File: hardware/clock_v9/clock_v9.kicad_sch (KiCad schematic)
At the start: 176 parts, among them J1 RJ45, J12 Conn_01x06, J14 DC-063-25A, J4 USB_C_Receptacle, J5 Conn_01x06_Pin, J6 Conn_01x04_Pin, J8 Conn_01x02, Q1 2N7002, Q10 2N7002, Q2 S8550, Q3 S8050, Q4 S8050, Q5 S8050, Q9 2N7002, SW1 LC1258OASP, U1 ADA4807-1, U10 STM32F405RGTx, U11 AMS1117-3.3, U12 BA50DD0WHFP-TR, U13 M24C02-RMN, U14 CH340C, U15 USBLC6-2P6, U16 TLV3603DCKR, U17 SN74LVC1G14DBV, U2 SN74LVC1G14DBV, U3 SN74LVC1G14DBV, U4 ADA4807-1, U5 ADA4807-1, U6 TLV3603DCKR, U7 SN74LVC1G14DBV, U8 TLV3603DCKR, U9 L78L05_SOT89, Y1 AOCJY4A-10.000MHZ-SW, Y2 16MHz

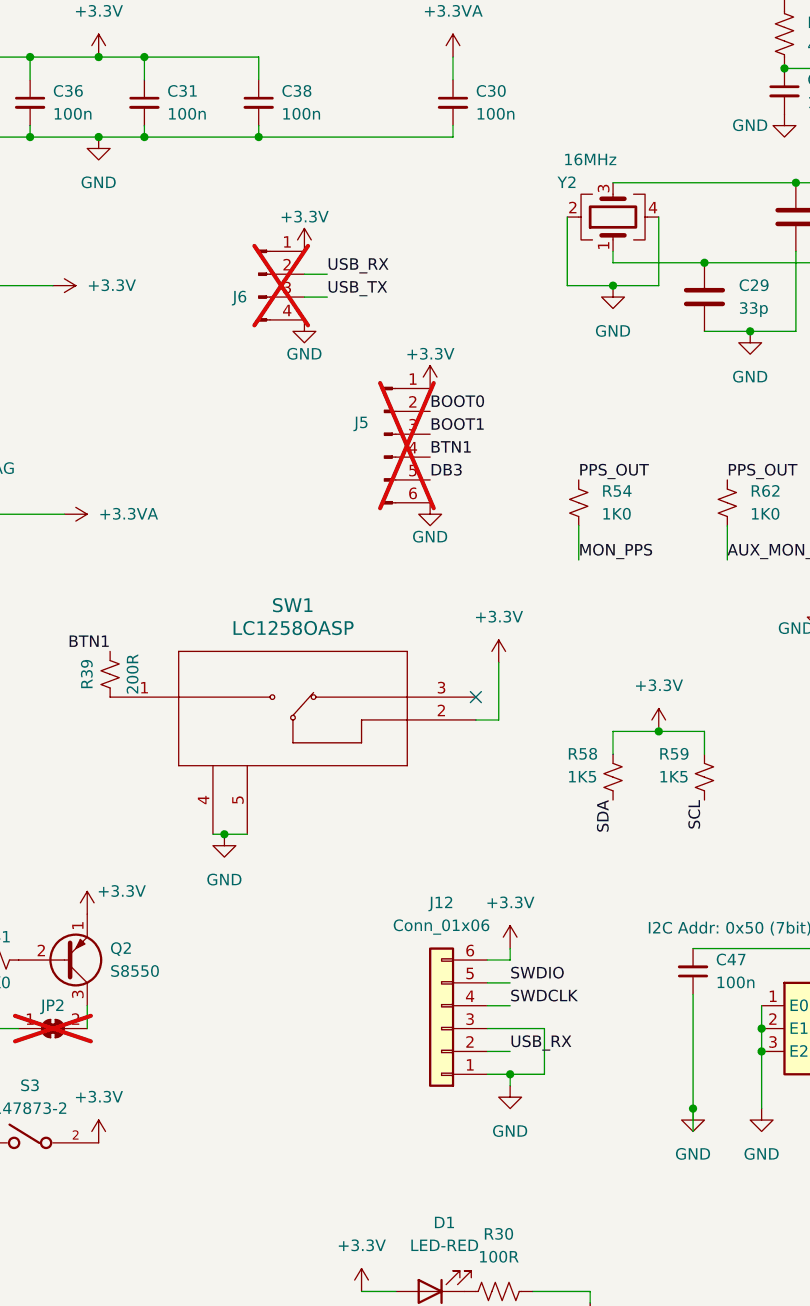
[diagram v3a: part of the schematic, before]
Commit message: update jumpers and swtiches
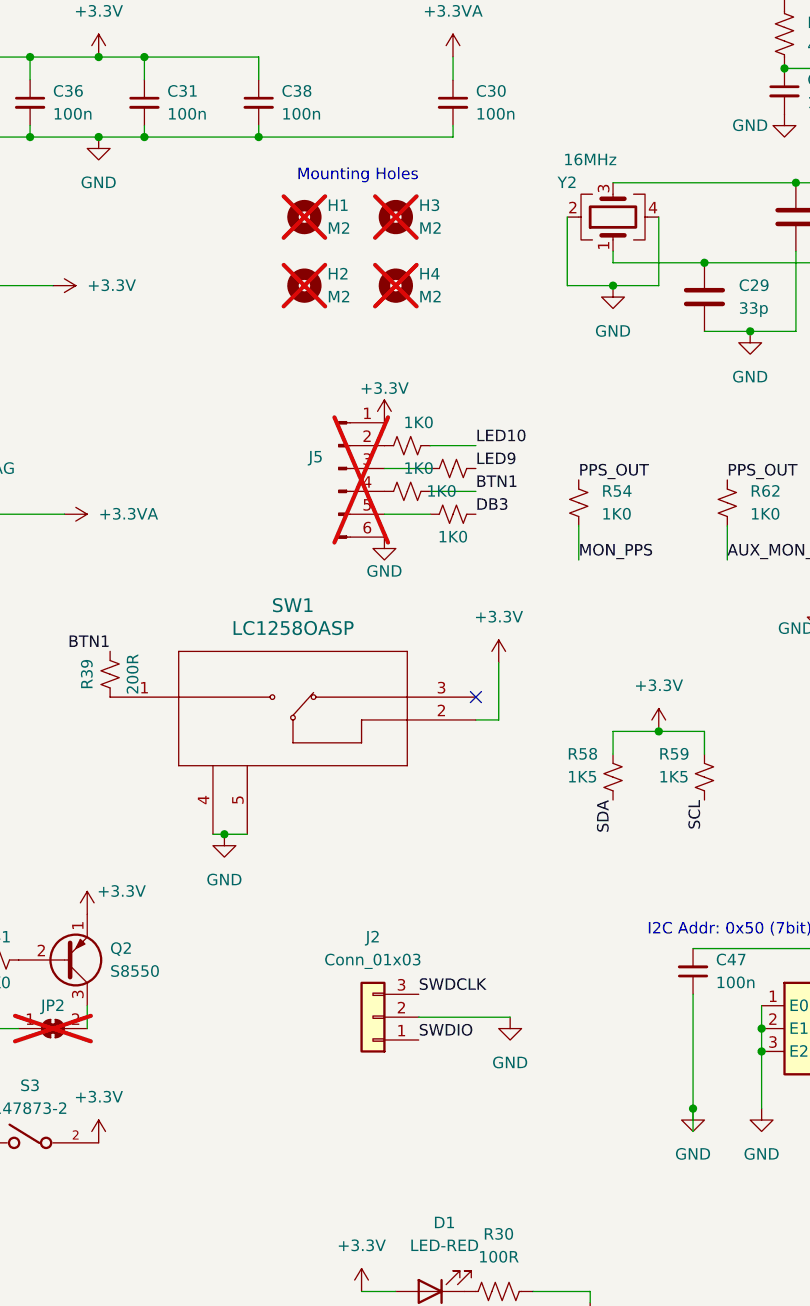
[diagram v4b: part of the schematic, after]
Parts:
- removed J12: Conn_01x06, Connector_JST:JST_PH_S6B-PH-SM4-TB_1x06-1MP_P2.00mm_Horizontal, symbol Connector_Generic:Conn_01x06
- removed J6: Conn_01x04_Pin, Connector_PinHeader_2.54mm:PinHeader_1x04_P2.54mm_Vertical, symbol Connector:Conn_01x04_Pin
- added H1, H2, H3, H4: M2, MountingHole:MountingHole_2.2mm_M2, symbol Mechanical:MountingHole
- added J2: Conn_01x03, Connector_JST:JST_PH_S3B-PH-SM4-TB_1x03-1MP_P2.00mm_Horizontal, symbol Connector_Generic:Conn_01x03
- added R65, R66, R67, R68: 1K0, Resistor_SMD:R_0603_1608Metric, symbol Device:R_Small_US
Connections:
- net BOOT0: no longer J5.2 (Pin_2)
- net BOOT1: no longer J5.3 (Pin_3)
- net BTN1: now also R66.1; no longer J5.4 (Pin_4)
- net DB3: now also R68.1; no longer J5.5 (Pin_5)
- net GND: now also J2.2 (Pin_2)
- net LED10: now also R65.1
- net LED9: now also R67.1
- net SWDCLK: now also J2.3 (Pin_3)
- net SWDIO: now also J2.1 (Pin_1)
- new net: J5.3 (Pin_3), R67.2
- new net: J5.4 (Pin_4), R66.2
- new net: J5.5 (Pin_5), R68.2
- new net: J5.2 (Pin_2), R65.2
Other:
- note added: "Mounting Holes"

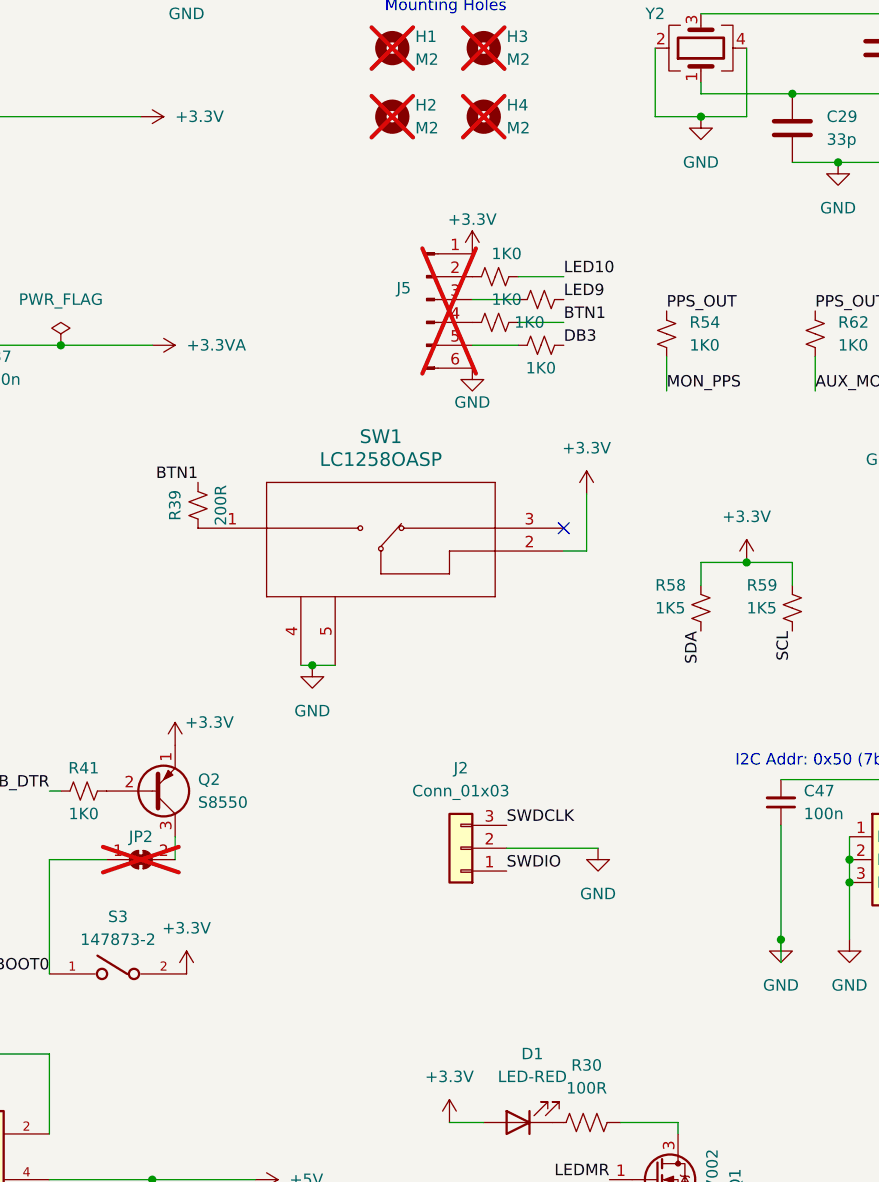
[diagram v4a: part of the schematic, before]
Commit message: add temp sensor
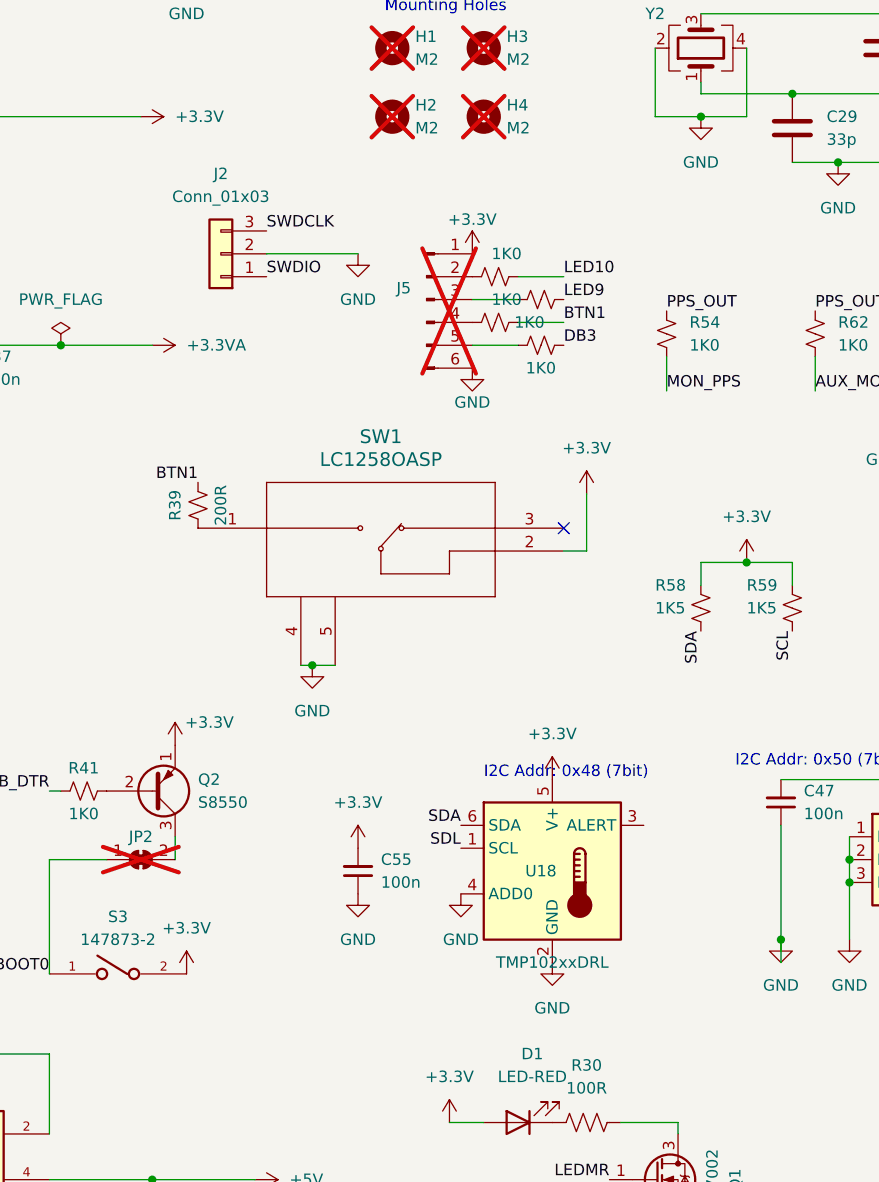
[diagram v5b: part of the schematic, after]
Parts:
- added C55: 100n, Capacitor_SMD:C_0402_1005Metric, symbol Device:C_Small
- added U18: TMP102xxDRL, Package_TO_SOT_SMD:SOT-563, symbol Sensor_Temperature:TMP102xxDRL
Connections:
- net +3.3V: now also C55.2, U18.5 (V+)
- net GND: now also C55.1, U18.2 (GND), U18.4 (ADD0)
- net SDA: now also U18.6 (SDA)
- new net SDL: U18.1 (SCL)
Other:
- note added: "I2C Addr: 0x48 (7bit)"
- moved on the sheet: J2
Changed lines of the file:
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@@
     (stroke (width 0) (type default))
   )
-  (wire (pts (xy 113.03 134.62) (xy 123.19 134.62))
+  (wire (pts (xy 86.36 68.58) (xy 96.52 68.58))
     (stroke (width 0) (type default))
   )
@@
     (effects (font (size 1.27 1.27)) (justify left bottom))
   )
+  (text "I2C Addr: 0x48 (7bit)" (at 110.49 127 0)
+    (effects (font (size 1.27 1.27)) (justify left bottom))
+  )
   (text "I2C Addr: 0x50 (7bit)" (at 138.43 125.73 0)
     (effects (font (size 1.27 1.27)) (justify left bottom))
@@
     (effects (font (size 1.27 1.27)) (justify right bottom))
   )
-  (label "SWDIO" (at 113.03 137.16 0) (fields_autoplaced)
+  (label "SWDIO" (at 86.36 71.12 0) (fields_autoplaced)
     (effects (font (size 1.27 1.27)) (justify left bottom))
   )
@@
     (effects (font (size 1.27 1.27)) (justify right bottom))
   )
+  (label "SDL" (at 107.95 134.62 180) (fields_autoplaced)
+    (effects (font (size 1.27 1.27)) (justify right bottom))
+  )
   (label "NCOL10" (at 177.8 91.44 180) (fields_autoplaced)
     (effects (font (size 1.27 1.27)) (justify right bottom))
@@
     (effects (font (size 1.27 1.27)) (justify right bottom))
   )
-  (label "SWDCLK" (at 113.03 132.08 0) (fields_autoplaced)
+  (label "SWDCLK" (at 86.36 66.04 0) (fields_autoplaced)
     (effects (font (size 1.27 1.27)) (justify left bottom))
   )
@@
     (effects (font (size 1.27 1.27)) (justify right bottom))
   )
+  (label "SDA" (at 107.95 132.08 180) (fields_autoplaced)
+    (effects (font (size 1.27 1.27)) (justify right bottom))
+  )
   (label "GPS_TX1H" (at 151.13 181.61 180) (fields_autoplaced)
     (effects (font (size 1.27 1.27)) (justify right bottom))
@@
     )
   )
+  (symbol (lib_id "power:GND") (at 96.52 139.7 0) (unit 1)
+    (in_bom yes) (on_board yes) (dnp no)
+    (property "Reference" "#PWR023" (at 96.52 146.05 0)
+      (effects (font (size 1.27 1.27)) hide)
+    )
+    (property "Value" "GND" (at 96.52 144.78 0)
+      (effects (font (size 1.27 1.27)))
+    )
+    (property "Footprint" "" (at 96.52 139.7 0)
+      (effects (font (size 1.27 1.27)) hide)
+    )
+    (property "Datasheet" "" (at 96.52 139.7 0)
+      (effects (font (size 1.27 1.27)) hide)
+    )
+    (pin "1")
+    (instances
+      (project "clock_v9"
+        (path "/bd4d3b9a-07c1-4a53-9c94-2893f3e869d4"
+          (reference "#PWR023") (unit 1)
+        )
+      )
+    )
+  )
   (symbol (lib_id "Device:R_Small_US") (at 111.76 76.2 270) (unit 1)
     (in_bom yes) (on_board yes) (dnp no)
@@
     )
   )
-  (symbol (lib_id "Connector_Generic:Conn_01x03") (at 107.95 134.62 180) (unit 1)
+  (symbol (lib_id "Connector_Generic:Conn_01x03") (at 81.28 68.58 180) (unit 1)
     (in_bom yes) (on_board yes) (dnp no) (fields_autoplaced)
-    (property "Reference" "J2" (at 107.95 125.73 0)
+    (property "Reference" "J2" (at 81.28 59.69 0)
       (effects (font (size 1.27 1.27)))
     )
-    (property "Value" "Conn_01x03" (at 107.95 128.27 0)
+    (property "Value" "Conn_01x03" (at 81.28 62.23 0)
       (effects (font (size 1.27 1.27)))
     )
-    (property "Footprint" "Connector_JST:JST_PH_S3B-PH-SM4-TB_1x03-1MP_P2.00mm_Horizontal" (at 107.95 134.62 0)
+    (property "Footprint" "Connector_JST:JST_PH_S3B-PH-SM4-TB_1x03-1MP_P2.00mm_Horizontal" (at 81.28 68.58 0)
       (effects (font (size 1.27 1.27)) hide)
     )
-    (property "Datasheet" "~" (at 107.95 134.62 0)
+    (property "Datasheet" "~" (at 81.28 68.58 0)
       (effects (font (size 1.27 1.27)) hide)
     )
@@
     )
   )
+  (symbol (lib_id "Device:C_Small") (at 96.52 137.16 180) (unit 1)
+    (in_bom yes) (on_board yes) (dnp no) (fields_autoplaced)
+    (property "Reference" "C55" (at 99.06 135.8836 0)
+      (effects (font (size 1.27 1.27)) (justify right))
+    )
+    (property "Value" "100n" (at 99.06 138.4236 0)
+      (effects (font (size 1.27 1.27)) (justify right))
+    )
+    (property "Footprint" "Capacitor_SMD:C_0402_1005Metric" (at 96.52 137.16 0)
+      (effects (font (size 1.27 1.27)) hide)
+    )
+    (property "Datasheet" "https://www.mouser.ca/datasheet/2/447/UPY_GPHC_X7R_6_3V_to_250V_23-3084653.pdf" (at 96.52 137.16 0)
+      (effects (font (size 1.27 1.27)) hide)
+    )
+    (property "LCSC" "" (at 96.52 137.16 0)
+      (effects (font (size 1.27 1.27)) hide)
+    )
+    (property "JLCPCB Part #" "C307331" (at 96.52 137.16 0)
+      (effects (font (size 1.27 1.27)) hide)
+    )
+    (pin "1")
+    (pin "2")
+    (instances
+      (project "clock_v9"
+        (path "/bd4d3b9a-07c1-4a53-9c94-2893f3e869d4"
+          (reference "C55") (unit 1)
+        )
+      )
+    )
+  )
   (symbol (lib_id "Device:R_US") (at 186.69 231.14 270) (mirror x) (unit 1)
     (in_bom yes) (on_board yes) (dnp no)
@@
     )
   )
+  (symbol (lib_id "power:+3.3V") (at 96.52 134.62 0) (unit 1)
+    (in_bom yes) (on_board yes) (dnp no) (fields_autoplaced)
+    (property "Reference" "#PWR021" (at 96.52 138.43 0)
+      (effects (font (size 1.27 1.27)) hide)
+    )
+    (property "Value" "+3.3V" (at 96.52 129.54 0)
+      (effects (font (size 1.27 1.27)))
+    )
+    (property "Footprint" "" (at 96.52 134.62 0)
+      (effects (font (size 1.27 1.27)) hide)
+    )
+    (property "Datasheet" "" (at 96.52 134.62 0)
+      (effects (font (size 1.27 1.27)) hide)
+    )
+    (pin "1")
+    (instances
+      (project "clock_v9"
+        (path "/bd4d3b9a-07c1-4a53-9c94-2893f3e869d4"
+          (reference "#PWR021") (unit 1)
+        )
+      )
+    )
+  )
   (symbol (lib_id "power:GND") (at 283.21 22.86 0) (mirror y) (unit 1)
     (in_bom yes) (on_board yes) (dnp no)
@@
     )
   )
-  (symbol (lib_id "power:GND") (at 123.19 134.62 0) (unit 1)
+  (symbol (lib_id "power:GND") (at 96.52 68.58 0) (unit 1)
     (in_bom yes) (on_board yes) (dnp no) (fields_autoplaced)
-    (property "Reference" "#PWR0102" (at 123.19 140.97 0)
+    (property "Reference" "#PWR0102" (at 96.52 74.93 0)
       (effects (font (size 1.27 1.27)) hide)
     )
-    (property "Value" "GND" (at 123.19 139.7 0)
+    (property "Value" "GND" (at 96.52 73.66 0)
       (effects (font (size 1.27 1.27)))
     )
-    (property "Footprint" "" (at 123.19 134.62 0)
+    (property "Footprint" "" (at 96.52 68.58 0)
       (effects (font (size 1.27 1.27)) hide)
     )
-    (property "Datasheet" "" (at 123.19 134.62 0)
+    (property "Datasheet" "" (at 96.52 68.58 0)
       (effects (font (size 1.27 1.27)) hide)
     )
@@
     )
   )
+  (symbol (lib_id "Sensor_Temperature:TMP102xxDRL") (at 118.11 137.16 0) (unit 1)
+    (in_bom yes) (on_board yes) (dnp no)
+    (property "Reference" "U18" (at 116.84 137.16 0)
+      (effects (font (size 1.27 1.27)))
+    )
+    (property "Value" "TMP102xxDRL" (at 118.11 147.32 0)
+      (effects (font (size 1.27 1.27)))
+    )
+    (property "Footprint" "Package_TO_SOT_SMD:SOT-563" (at 119.38 146.05 0)
+      (effects (font (size 1.27 1.27)) (justify left) hide)
+    )
+    (property "Datasheet" "https://www.ti.com/lit/ds/symlink/tmp102.pdf" (at 119.38 148.59 0)
+      (effects (font (size 1.27 1.27)) (justify left) hide)
+    )
+    (pin "1")
+    (pin "2")
+    (pin "3")
+    (pin "4")
+    (pin "5")
+    (pin "6")
+    (instances
+      (project "clock_v9"
+        (path "/bd4d3b9a-07c1-4a53-9c94-2893f3e869d4"
+          (reference "U18") (unit 1)
+        )
+      )
+    )
+  )
   (symbol (lib_id "Device:R_Small_US") (at 116.84 78.74 270) (unit 1)
     (in_bom yes) (on_board yes) (dnp no)
@@
     )
   )
+  (symbol (lib_id "power:+3.3V") (at 118.11 127 0) (unit 1)
+    (in_bom yes) (on_board yes) (dnp no) (fields_autoplaced)
+    (property "Reference" "#PWR0124" (at 118.11 130.81 0)
+      (effects (font (size 1.27 1.27)) hide)
+    )
+    (property "Value" "+3.3V" (at 118.11 121.92 0)
+      (effects (font (size 1.27 1.27)))
+    )
+    (property "Footprint" "" (at 118.11 127 0)
+      (effects (font (size 1.27 1.27)) hide)
+    )
+    (property "Datasheet" "" (at 118.11 127 0)
+      (effects (font (size 1.27 1.27)) hide)
+    )
+    (pin "1")
+    (instances
+      (project "clock_v9"
+        (path "/bd4d3b9a-07c1-4a53-9c94-2893f3e869d4"
+          (reference "#PWR0124") (unit 1)
+        )
+      )
+    )
+  )
   (symbol (lib_id "Diode:1N4148W") (at 163.83 177.8 90) (unit 1)
     (in_bom yes) (on_board yes) (dnp no) (fields_autoplaced)
@@
     )
   )
+  (symbol (lib_id "power:GND") (at 118.11 147.32 0) (unit 1)
+    (in_bom yes) (on_board yes) (dnp no)
+    (property "Reference" "#PWR0128" (at 118.11 153.67 0)
+      (effects (font (size 1.27 1.27)) hide)
+    )
+    (property "Value" "GND" (at 118.11 152.4 0)
+      (effects (font (size 1.27 1.27)))
+    )
+    (property "Footprint" "" (at 118.11 147.32 0)
+      (effects (font (size 1.27 1.27)) hide)
+    )
+    (property "Datasheet" "" (at 118.11 147.32 0)
+      (effects (font (size 1.27 1.27)) hide)
+    )
+    (pin "1")
+    (instances
+      (project "clock_v9"
+        (path "/bd4d3b9a-07c1-4a53-9c94-2893f3e869d4"
+          (reference "#PWR0128") (unit 1)
+        )
+      )
+    )
+  )
   (symbol (lib_id "Device:C_Small") (at 379.73 151.13 0) (unit 1)
     (in_bom yes) (on_board yes) (dnp no)
@@
         )
       )
+    )
+  )
+  (symbol (lib_id "power:GND") (at 107.95 139.7 0) (unit 1)
+    (in_bom yes) (on_board yes) (dnp no)
+    (property "Reference" "#PWR0103" (at 107.95 146.05 0)
+      (effects (font (size 1.27 1.27)) hide)
+    )
+    (property "Value" "GND" (at 107.95 144.78 0)
+      (effects (font (size 1.27 1.27)))
+    )
+    (property "Footprint" "" (at 107.95 139.7 0)
+      (effects (font (size 1.27 1.27)) hide)
+    )
+    (property "Datasheet" "" (at 107.95 139.7 0)
+      (effects (font (size 1.27 1.27)) hide)
+    )
+    (pin "1")
+    (instances
+      (project "clock_v9"
+        (path "/bd4d3b9a-07c1-4a53-9c94-2893f3e869d4"
+          (reference "#PWR0103") (unit 1)
+        )
+      )

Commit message: start USB power mon
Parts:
- added JP4: SolderJumper_2_Bridged, Jumper:SolderJumper-2_P1.3mm_Bridged2Bar_RoundedPad1.0x1.5mm, symbol Jumper:SolderJumper_2_Bridged
- added R69, R70, R71: 1K0, Resistor_SMD:R_0603_1608Metric, symbol Device:R_Small_US
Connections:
- net SDL is gone; now on net SCL: U18.1 (SCL)
- net +5V: now also JP4.2 (B); no longer U12.4 (OUT)
- net +6V: no longer U12.1 (CTL)
- net AUD_IN: now also R70.1, R71.2
- net GND: now also R70.2
- net LED1: now also R69.2
- new net: JP4.1 (A), U12.4 (OUT)
- new net: R69.1, U12.1 (CTL)
- no-connect marks 35 -> 34
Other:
- moved on the sheet: C44
